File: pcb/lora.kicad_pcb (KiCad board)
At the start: 4 copper layers, 101.9 x 45.1 mm, 90 parts, among them J1 Conn_01x04, J11 Conn_Coaxial, J2 5V, J3 Conn_01x06, J4 USB_C_Receptacle_USB2.0, J5 Temp, J6 VDD, J7 UART, J8 Conn_01x04, J9 Conn_01x07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

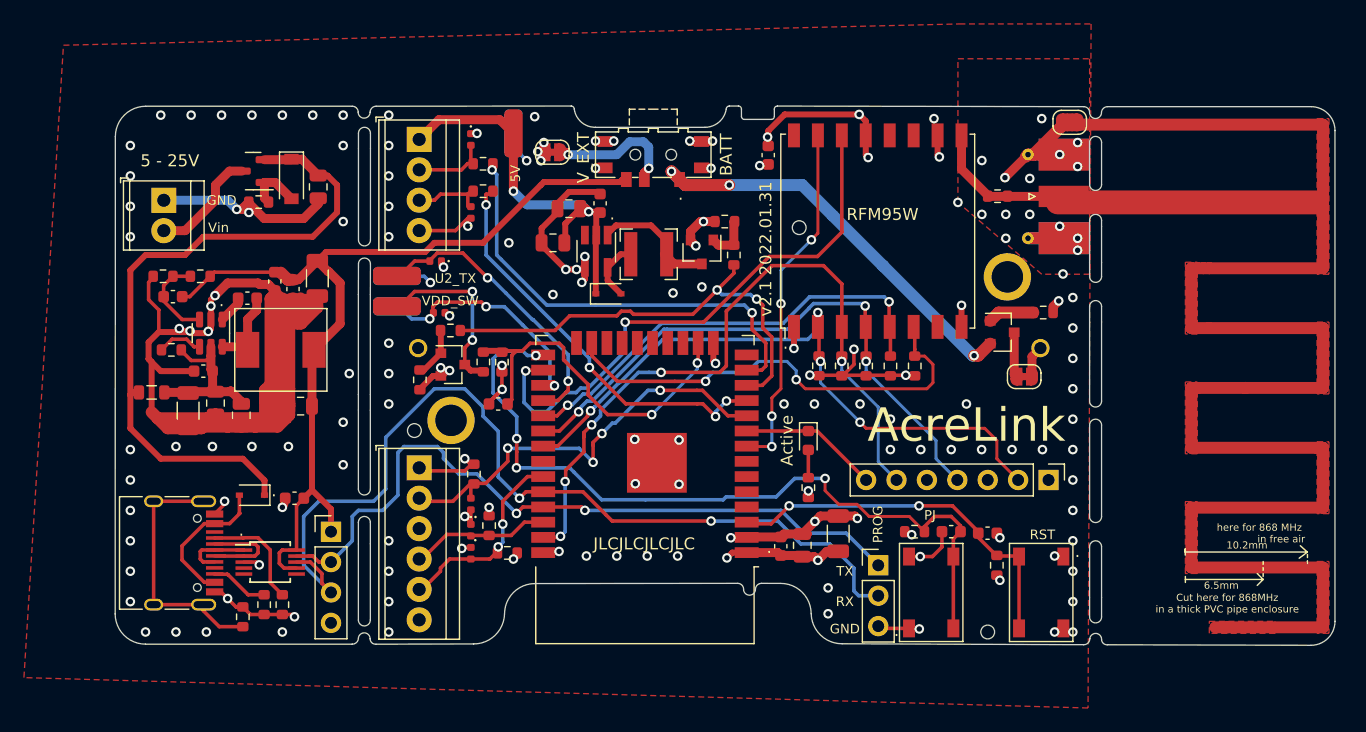
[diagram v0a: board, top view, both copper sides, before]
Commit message: v2.2 finalized, spi connector added and ground current measurement solder jumper added
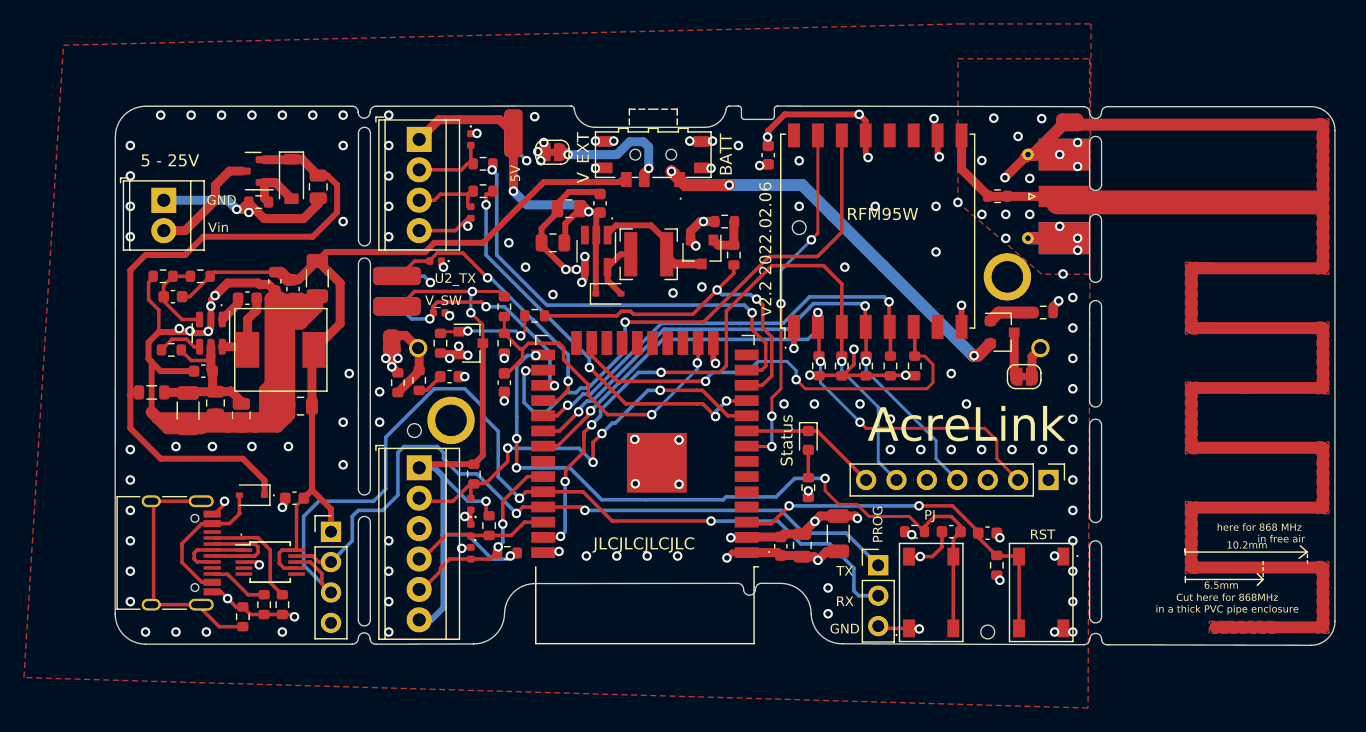
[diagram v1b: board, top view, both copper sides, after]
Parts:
- added C12: 100n, Capacitor_SMD:C_0603_1608Metric, F.Cu at (176.5, 114.6)
- added JP4: ISense_GND, Jumper:SolderJumper-2_P1.3mm_Bridged_RoundedPad1.0x1.5mm, F.Cu at (171.7, 111.8)
- added R28: 10k, Resistor_SMD:R_0603_1608Metric, F.Cu at (174.0, 114.9)
- added R29: 1R, Resistor_SMD:R_0603_1608Metric, F.Cu at (172.2, 115.1)
- moved R10 7.15 mm to (183.6, 109.5)
- moved R7 4.94 mm to (181.1, 108.7), turned to 90 degrees
- moved R9 3.51 mm to (175.8, 111.8)
- moved Q2 2.34 mm to (178.3, 111.8)
- moved C2 1.85 mm to (181.1, 115.1), turned to 90 degrees
- moved R8 1.59 mm to (181.1, 111.8)
- moved J4 0.20 mm to (152.7, 129.3)
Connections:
- J3 pad 1: VDD -> VDD_SWITCHED
- J3 pad 6: VDD -> VDD_SWITCHED
- R15 pad 1: VDD -> VDD_SWITCHED
- R16 pad 1: VDD -> VDD_SWITCHED
- R20 pad 1: VDD -> VDD_SWITCHED
- U3 pad 2: GND -> Net-(U3-Pad2)
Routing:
- net VDD_SWITCHED: track 15.0 -> 58.3 mm, vias 2 -> 4
- net POWER_EN: track 38.7 -> 31.2 mm
- net Net-(U3-Pad2): track 0.00 -> 7.13 mm
- net VDD: track 55.4 -> 48.8 mm, vias 22 -> 20
- net Net-(Q2-Pad1): track 4.26 -> 8.77 mm, vias 0 -> 2
- net PRG_JP: track 65.9 -> 62.4 mm
- net Net-(C12-Pad2): track 0.00 -> 2.24 mm
- net VDD_SENSE: track 30.0 -> 28.5 mm
- net Net-(D11-Pad2): track 12.2 -> 12.9 mm
- net Net-(J4-PadA6): track 5.63 -> 6.17 mm
- net GND: track 230.4 -> 230.5 mm, vias 143 -> 157
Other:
- board text added: "Status"
- board text added: "V_SW"
- board text added: "v2.2 2022.02.06"
- board text removed: "Active"
- board text removed: "VDD_SW"
- board text removed: "v2.1 2022.01.31"

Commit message: added mouse bites for breakaway tabs
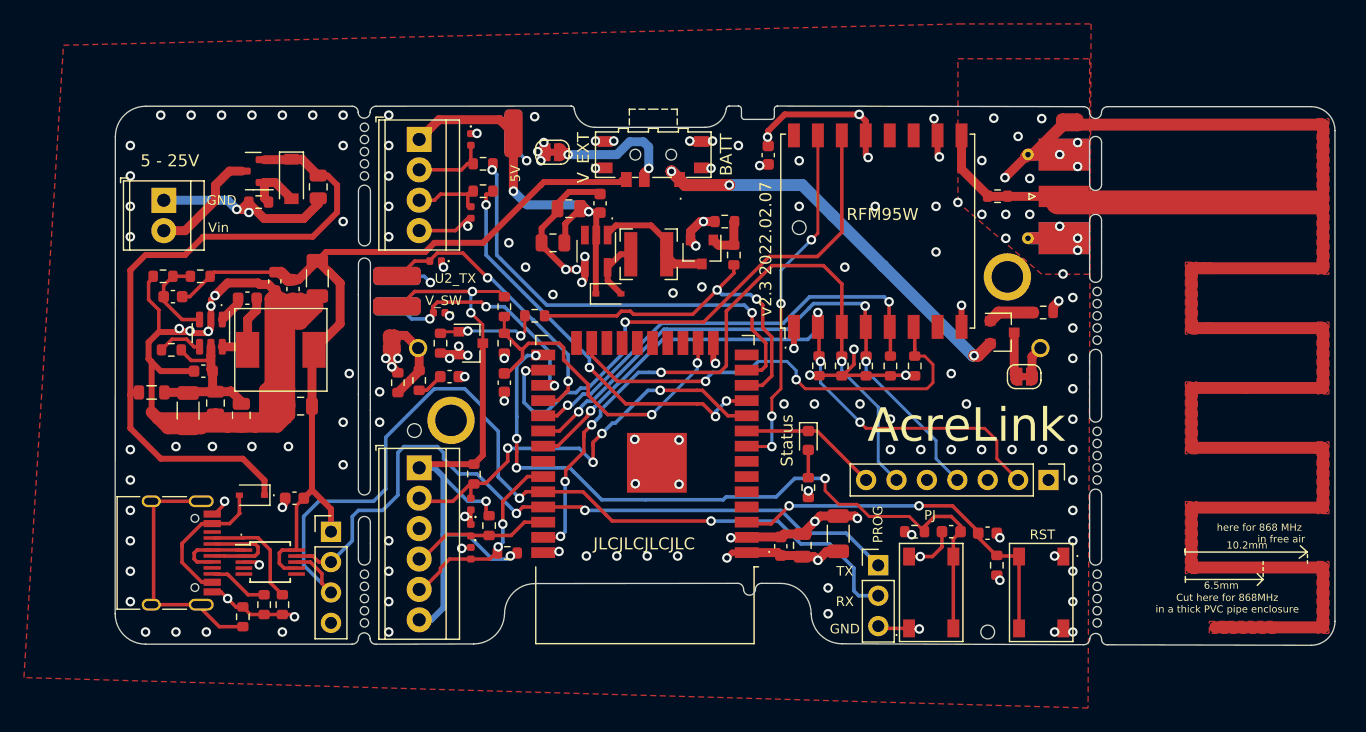
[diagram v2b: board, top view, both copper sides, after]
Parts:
- added REF**: mouse_bite_hole_0.7mm, OWN_Parts_:mouse_bite_hole_0.7mm, F.Cu at (169.4, 133.1)
- added REF**: mouse_bite_hole_0.7mm, OWN_Parts_:mouse_bite_hole_0.7mm, F.Cu at (169.4, 132.1)
- added REF**: mouse_bite_hole_0.7mm, OWN_Parts_:mouse_bite_hole_0.7mm, F.Cu at (230.6, 108.5)
- added REF**: mouse_bite_hole_0.7mm, OWN_Parts_:mouse_bite_hole_0.7mm, F.Cu at (169.4, 97.8)
- added REF**: mouse_bite_hole_0.7mm, OWN_Parts_:mouse_bite_hole_0.7mm, F.Cu at (230.6, 135.1)
- added REF**: mouse_bite_hole_0.7mm, OWN_Parts_:mouse_bite_hole_0.7mm, F.Cu at (169.4, 131.1)
- added REF**: mouse_bite_hole_0.7mm, OWN_Parts_:mouse_bite_hole_0.7mm, F.Cu at (230.6, 134.1)
- added REF**: mouse_bite_hole_0.7mm, OWN_Parts_:mouse_bite_hole_0.7mm, F.Cu at (230.6, 123.2)
- added REF**: mouse_bite_hole_0.7mm, OWN_Parts_:mouse_bite_hole_0.7mm, F.Cu at (230.6, 121.2)
- added REF**: mouse_bite_hole_0.7mm, OWN_Parts_:mouse_bite_hole_0.7mm, F.Cu at (169.4, 94.7)
- added REF**: mouse_bite_hole_0.7mm, OWN_Parts_:mouse_bite_hole_0.7mm, F.Cu at (230.6, 119.1)
- added REF**: mouse_bite_hole_0.7mm, OWN_Parts_:mouse_bite_hole_0.7mm, F.Cu at (169.4, 96.8)
- added REF**: mouse_bite_hole_0.7mm, OWN_Parts_:mouse_bite_hole_0.7mm, F.Cu at (230.6, 133.1)
- added REF**: mouse_bite_hole_0.7mm, OWN_Parts_:mouse_bite_hole_0.7mm, F.Cu at (230.6, 111.5)
- added REF**: mouse_bite_hole_0.7mm, OWN_Parts_:mouse_bite_hole_0.7mm, F.Cu at (230.6, 122.2)
- added REF**: mouse_bite_hole_0.7mm, OWN_Parts_:mouse_bite_hole_0.7mm, F.Cu at (230.6, 131.1)
- added REF**: mouse_bite_hole_0.7mm, OWN_Parts_:mouse_bite_hole_0.7mm, F.Cu at (169.4, 135.1)
- added REF**: mouse_bite_hole_0.7mm, OWN_Parts_:mouse_bite_hole_0.7mm, F.Cu at (169.4, 93.7)
- added REF**: mouse_bite_hole_0.7mm, OWN_Parts_:mouse_bite_hole_0.7mm, F.Cu at (230.6, 110.5)
- added REF**: mouse_bite_hole_0.7mm, OWN_Parts_:mouse_bite_hole_0.7mm, F.Cu at (230.6, 109.5)
- added REF**: mouse_bite_hole_0.7mm, OWN_Parts_:mouse_bite_hole_0.7mm, F.Cu at (230.6, 107.4)
- added REF**: mouse_bite_hole_0.7mm, OWN_Parts_:mouse_bite_hole_0.7mm, F.Cu at (230.6, 132.1)
- added REF**: mouse_bite_hole_0.7mm, OWN_Parts_:mouse_bite_hole_0.7mm, F.Cu at (230.6, 120.1)
- added REF**: mouse_bite_hole_0.7mm, OWN_Parts_:mouse_bite_hole_0.7mm, F.Cu at (169.4, 95.8)
- added REF**: mouse_bite_hole_0.7mm, OWN_Parts_:mouse_bite_hole_0.7mm, F.Cu at (169.4, 134.1)
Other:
- outline, holes or cut-outs redrawn
- board text added: "v2.3 2022.02.07"
- board text removed: "v2.2 2022.02.06"
